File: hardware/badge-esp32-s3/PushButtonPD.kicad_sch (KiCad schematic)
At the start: 4 parts

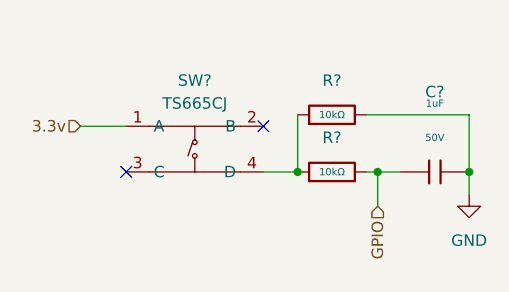
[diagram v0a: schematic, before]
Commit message: update labels for changes
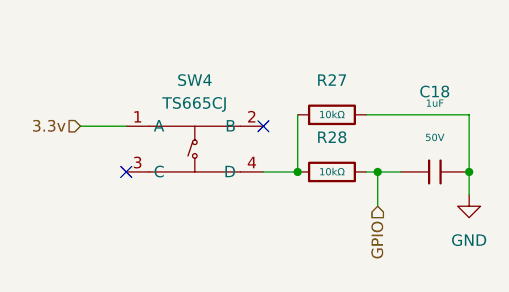
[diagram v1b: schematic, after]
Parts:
- gave numbers to parts that had none: 4
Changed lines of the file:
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@@
 		(dnp no)
 		(fields_autoplaced yes)
-		(property "Reference" "SW?"
+		(property "Reference" "SW4"
 			(at 120.65 71.12 0)
 			(effects
@@
 				(path "/3df4ba36-75c7-47ee-bf08-afd9250f8b93"
 					(reference "SW?")
+					(unit 1)
+				)
+			)
+			(project "badge-esp32-s3"
+				(path "/e2af9a6c-dbe9-4de2-9ba6-ea213a7300ec/9feb22ac-0492-47b5-89fe-3e77a54de168/0c6f020c-1e0e-43cd-8a36-0a56f6d3220b"
+					(reference "SW6")
+					(unit 1)
+				)
+				(path "/e2af9a6c-dbe9-4de2-9ba6-ea213a7300ec/9feb22ac-0492-47b5-89fe-3e77a54de168/26f14f73-3c64-431d-bfa5-e30d3515d6c4"
+					(reference "SW9")
+					(unit 1)
+				)
+				(path "/e2af9a6c-dbe9-4de2-9ba6-ea213a7300ec/9feb22ac-0492-47b5-89fe-3e77a54de168/a24e4638-e764-42f8-9a03-a3574c3b6e5b"
+					(reference "SW4")
+					(unit 1)
+				)
+				(path "/e2af9a6c-dbe9-4de2-9ba6-ea213a7300ec/9feb22ac-0492-47b5-89fe-3e77a54de168/b99b1c65-2141-4657-af08-7b837c45a510"
+					(reference "SW5")
+					(unit 1)
+				)
+				(path "/e2af9a6c-dbe9-4de2-9ba6-ea213a7300ec/9feb22ac-0492-47b5-89fe-3e77a54de168/f11ff8f0-58bf-4f8c-9221-02eb2354874a"
+					(reference "SW7")
+					(unit 1)
+				)
+				(path "/e2af9a6c-dbe9-4de2-9ba6-ea213a7300ec/9feb22ac-0492-47b5-89fe-3e77a54de168/fb6d2a04-654d-4115-8ed9-b9891bab072c"
+					(reference "SW8")
 					(unit 1)
 				)
@@
 		(dnp no)
 		(fields_autoplaced yes)
-		(property "Reference" "#PWR?"
+		(property "Reference" "#PWR0104"
 			(at 151.13 90.17 0)
 			(effects
@@
 				(path "/3df4ba36-75c7-47ee-bf08-afd9250f8b93"
 					(reference "#PWR?")
+					(unit 1)
+				)
+			)
+			(project "badge-esp32-s3"
+				(path "/e2af9a6c-dbe9-4de2-9ba6-ea213a7300ec/9feb22ac-0492-47b5-89fe-3e77a54de168/0c6f020c-1e0e-43cd-8a36-0a56f6d3220b"
+					(reference "#PWR0106")
+					(unit 1)
+				)
+				(path "/e2af9a6c-dbe9-4de2-9ba6-ea213a7300ec/9feb22ac-0492-47b5-89fe-3e77a54de168/26f14f73-3c64-431d-bfa5-e30d3515d6c4"
+					(reference "#PWR0109")
+					(unit 1)
+				)
+				(path "/e2af9a6c-dbe9-4de2-9ba6-ea213a7300ec/9feb22ac-0492-47b5-89fe-3e77a54de168/a24e4638-e764-42f8-9a03-a3574c3b6e5b"
+					(reference "#PWR0104")
+					(unit 1)
+				)
+				(path "/e2af9a6c-dbe9-4de2-9ba6-ea213a7300ec/9feb22ac-0492-47b5-89fe-3e77a54de168/b99b1c65-2141-4657-af08-7b837c45a510"
+					(reference "#PWR0105")
+					(unit 1)
+				)
+				(path "/e2af9a6c-dbe9-4de2-9ba6-ea213a7300ec/9feb22ac-0492-47b5-89fe-3e77a54de168/f11ff8f0-58bf-4f8c-9221-02eb2354874a"
+					(reference "#PWR0107")
+					(unit 1)
+				)
+				(path "/e2af9a6c-dbe9-4de2-9ba6-ea213a7300ec/9feb22ac-0492-47b5-89fe-3e77a54de168/fb6d2a04-654d-4115-8ed9-b9891bab072c"
+					(reference "#PWR0108")
 					(unit 1)
 				)
@@
 		(on_board yes)
 		(dnp no)
-		(property "Reference" "C?"
+		(property "Reference" "C18"
 			(at 147.32 72.39 90)
 			(effects
@@
 				(path "/3df4ba36-75c7-47ee-bf08-afd9250f8b93"
 					(reference "C?")
+					(unit 1)
+				)
+			)
+			(project "badge-esp32-s3"
+				(path "/e2af9a6c-dbe9-4de2-9ba6-ea213a7300ec/9feb22ac-0492-47b5-89fe-3e77a54de168/0c6f020c-1e0e-43cd-8a36-0a56f6d3220b"
+					(reference "C20")
+					(unit 1)
+				)
+				(path "/e2af9a6c-dbe9-4de2-9ba6-ea213a7300ec/9feb22ac-0492-47b5-89fe-3e77a54de168/26f14f73-3c64-431d-bfa5-e30d3515d6c4"
+					(reference "C23")
+					(unit 1)
+				)
+				(path "/e2af9a6c-dbe9-4de2-9ba6-ea213a7300ec/9feb22ac-0492-47b5-89fe-3e77a54de168/a24e4638-e764-42f8-9a03-a3574c3b6e5b"
+					(reference "C18")
+					(unit 1)
+				)
+				(path "/e2af9a6c-dbe9-4de2-9ba6-ea213a7300ec/9feb22ac-0492-47b5-89fe-3e77a54de168/b99b1c65-2141-4657-af08-7b837c45a510"
+					(reference "C19")
+					(unit 1)
+				)
+				(path "/e2af9a6c-dbe9-4de2-9ba6-ea213a7300ec/9feb22ac-0492-47b5-89fe-3e77a54de168/f11ff8f0-58bf-4f8c-9221-02eb2354874a"
+					(reference "C21")
+					(unit 1)
+				)
+				(path "/e2af9a6c-dbe9-4de2-9ba6-ea213a7300ec/9feb22ac-0492-47b5-89fe-3e77a54de168/fb6d2a04-654d-4115-8ed9-b9891bab072c"
+					(reference "C22")
 					(unit 1)
 				)
@@
 		(dnp no)
 		(fields_autoplaced yes)
-		(property "Reference" "R?"
+		(property "Reference" "R28"
 			(at 135.89 77.47 90)
 			(effects
@@
 				(path "/3df4ba36-75c7-47ee-bf08-afd9250f8b93"
 					(reference "R?")
+					(unit 1)
+				)
+			)
+			(project "badge-esp32-s3"
+				(path "/e2af9a6c-dbe9-4de2-9ba6-ea213a7300ec/9feb22ac-0492-47b5-89fe-3e77a54de168/0c6f020c-1e0e-43cd-8a36-0a56f6d3220b"
+					(reference "R32")
+					(unit 1)
+				)
+				(path "/e2af9a6c-dbe9-4de2-9ba6-ea213a7300ec/9feb22ac-0492-47b5-89fe-3e77a54de168/26f14f73-3c64-431d-bfa5-e30d3515d6c4"
+					(reference "R38")
+					(unit 1)
+				)
+				(path "/e2af9a6c-dbe9-4de2-9ba6-ea213a7300ec/9feb22ac-0492-47b5-89fe-3e77a54de168/a24e4638-e764-42f8-9a03-a3574c3b6e5b"
+					(reference "R28")
+					(unit 1)
+				)
+				(path "/e2af9a6c-dbe9-4de2-9ba6-ea213a7300ec/9feb22ac-0492-47b5-89fe-3e77a54de168/b99b1c65-2141-4657-af08-7b837c45a510"
+					(reference "R30")
+					(unit 1)
+				)
+				(path "/e2af9a6c-dbe9-4de2-9ba6-ea213a7300ec/9feb22ac-0492-47b5-89fe-3e77a54de168/f11ff8f0-58bf-4f8c-9221-02eb2354874a"
+					(reference "R34")
+					(unit 1)
+				)
+				(path "/e2af9a6c-dbe9-4de2-9ba6-ea213a7300ec/9feb22ac-0492-47b5-89fe-3e77a54de168/fb6d2a04-654d-4115-8ed9-b9891bab072c"
+					(reference "R36")
 					(unit 1)
 				)
@@
 		(dnp no)
 		(fields_autoplaced yes)
-		(property "Reference" "R?"
+		(property "Reference" "R27"
 			(at 135.89 71.12 90)
 			(effects
@@
 					(unit 1)
 				)
+			)
+			(project "badge-esp32-s3"
+				(path "/e2af9a6c-dbe9-4de2-9ba6-ea213a7300ec/9feb22ac-0492-47b5-89fe-3e77a54de168/0c6f020c-1e0e-43cd-8a36-0a56f6d3220b"
+					(reference "R31")
+					(unit 1)
+				)
+				(path "/e2af9a6c-dbe9-4de2-9ba6-ea213a7300ec/9feb22ac-0492-47b5-89fe-3e77a54de168/26f14f73-3c64-431d-bfa5-e30d3515d6c4"
+					(reference "R37")
+					(unit 1)
+				)
+				(path "/e2af9a6c-dbe9-4de2-9ba6-ea213a7300ec/9feb22ac-0492-47b5-89fe-3e77a54de168/a24e4638-e764-42f8-9a03-a3574c3b6e5b"
+					(reference "R27")
+					(unit 1)
+				)
+				(path "/e2af9a6c-dbe9-4de2-9ba6-ea213a7300ec/9feb22ac-0492-47b5-89fe-3e77a54de168/b99b1c65-2141-4657-af08-7b837c45a510"
+					(reference "R29")
+					(unit 1)
+				)
+				(path "/e2af9a6c-dbe9-4de2-9ba6-ea213a7300ec/9feb22ac-0492-47b5-89fe-3e77a54de168/f11ff8f0-58bf-4f8c-9221-02eb2354874a"
+					(reference "R33")
+					(unit 1)
+				)
+				(path "/e2af9a6c-dbe9-4de2-9ba6-ea213a7300ec/9feb22ac-0492-47b5-89fe-3e77a54de168/fb6d2a04-654d-4115-8ed9-b9891bab072c"
+					(reference "R35")
+					(unit 1)
+				)

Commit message: almost finished
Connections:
- net 3.3v: now also SW4.2 (B); no longer SW4.1 (A)
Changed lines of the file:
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@@
-	)
-	(no_connect
-		(at 128.27 76.2)
 	)
 	(no_connect
 		(at 113.03 81.28)
+	)
+	(no_connect
+		(at 113.03 76.2)
 	)
 	(wire
@@
 	(wire
 		(pts
-			(xy 107.95 76.2) (xy 113.03 76.2)
+			(xy 128.27 71.12) (xy 128.27 76.2)
 		)
 		(stroke
@@
 	(hierarchical_label "3.3v"
 		(shape input)
-		(at 107.95 76.2 180)
+		(at 128.27 71.12 90)
 		(effects
 			(font
 				(size 1.27 1.27)
 			)
-			(justify right)
+			(justify left)
 		)
 	)
@@
 					(unit 1)
 				)
-				(path "/e2af9a6c-dbe9-4de2-9ba6-ea213a7300ec/9feb22ac-0492-47b5-89fe-3e77a54de168/fb6d2a04-654d-4115-8ed9-b9891bab072c"
-					(reference "SW8")
-					(unit 1)
-				)
 			)
 		)
@@
 					(unit 1)
 				)
-				(path "/e2af9a6c-dbe9-4de2-9ba6-ea213a7300ec/9feb22ac-0492-47b5-89fe-3e77a54de168/fb6d2a04-654d-4115-8ed9-b9891bab072c"
-					(reference "#PWR0108")
-					(unit 1)
-				)
 			)
 		)
@@
 				(path "/e2af9a6c-dbe9-4de2-9ba6-ea213a7300ec/9feb22ac-0492-47b5-89fe-3e77a54de168/f11ff8f0-58bf-4f8c-9221-02eb2354874a"
 					(reference "C21")
-					(unit 1)
-				)
-				(path "/e2af9a6c-dbe9-4de2-9ba6-ea213a7300ec/9feb22ac-0492-47b5-89fe-3e77a54de168/fb6d2a04-654d-4115-8ed9-b9891bab072c"
-					(reference "C22")
 					(unit 1)
 				)
@@
 					(unit 1)
 				)
-				(path "/e2af9a6c-dbe9-4de2-9ba6-ea213a7300ec/9feb22ac-0492-47b5-89fe-3e77a54de168/fb6d2a04-654d-4115-8ed9-b9891bab072c"
-					(reference "R36")
-					(unit 1)
-				)
 			)
 		)
@@
 					(unit 1)
 				)
-				(path "/e2af9a6c-dbe9-4de2-9ba6-ea213a7300ec/9feb22ac-0492-47b5-89fe-3e77a54de168/fb6d2a04-654d-4115-8ed9-b9891bab072c"
-					(reference "R35")
-					(unit 1)
-				)
-			)
-		)
-	)
-	(sheet_instances
-		(path "/"
-			(page "1")
-		)
-	)
-	(embedded_fonts no)
+			)
+		)
+	)
 )
